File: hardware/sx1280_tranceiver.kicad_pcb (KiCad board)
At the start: 2 copper layers, 22 parts, among them J1 U.FL-R-SMT-1(80), J2 Conn_02x06_Odd_Even, U1 sx1280, U2 2450FM07D0034, Y1 ECS-520-12-37B-CTN-TR

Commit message: finalized layout
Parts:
- moved C9 2.80 mm to (84.7, 67.9)
- moved J1 2.80 mm to (86.1, 70.5)
- moved L1 2.80 mm to (86.1, 67.4)
- moved R2 2.80 mm to (86.1, 65.5)
- moved R3 2.80 mm to (86.6, 65.0)
- moved U2 2.80 mm to (84.5, 65.0)
- moved C10 2.56 mm to (89.3, 66.4)
- moved L2 2.56 mm to (88.8, 65.0)
- moved C5 2.38 mm to (80.8, 69.6)
- moved C3 2.35 mm to (79.8, 69.6)
- moved C1 2.32 mm to (78.9, 69.6)
- moved L3 2.20 mm to (76.5, 69.3)
- moved C7 2.20 mm to (79.1, 60.4)
- moved C8 2.20 mm to (75.5, 60.4)
- moved Y1 2.20 mm to (77.3, 60.4)
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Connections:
- J2 pad 12: ANT_SW -> unconnected-(J2-Pin_12-Pad12)
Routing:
- net SX_NSS: track 4.19 -> 35.5 mm
- net SX_SCK: track 3.72 -> 26.3 mm
- net SX_MOSI: track 3.84 -> 21.9 mm
- net SX_MISO: track 3.82 -> 18.2 mm
- net VBAT: track 29.2 -> 26.0 mm, vias 2 -> 1
- net Net-(AE1-FEED): track 2.49 -> 3.50 mm
- net VBAT_IO: track 4.85 -> 4.07 mm
- net Net-(U1-RFIO): track 2.72 -> 2.05 mm
- net GND: track 16.9 -> 16.7 mm, vias 11 -> 475
- added copper zone on In1.Cu, net GND
- added copper zone on In2.Cu, net GND
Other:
- board outline added: 30.5 x 16 mm
- copper layers 2 -> 4
- board text added: "sx1280_tranceiver by ihysol"

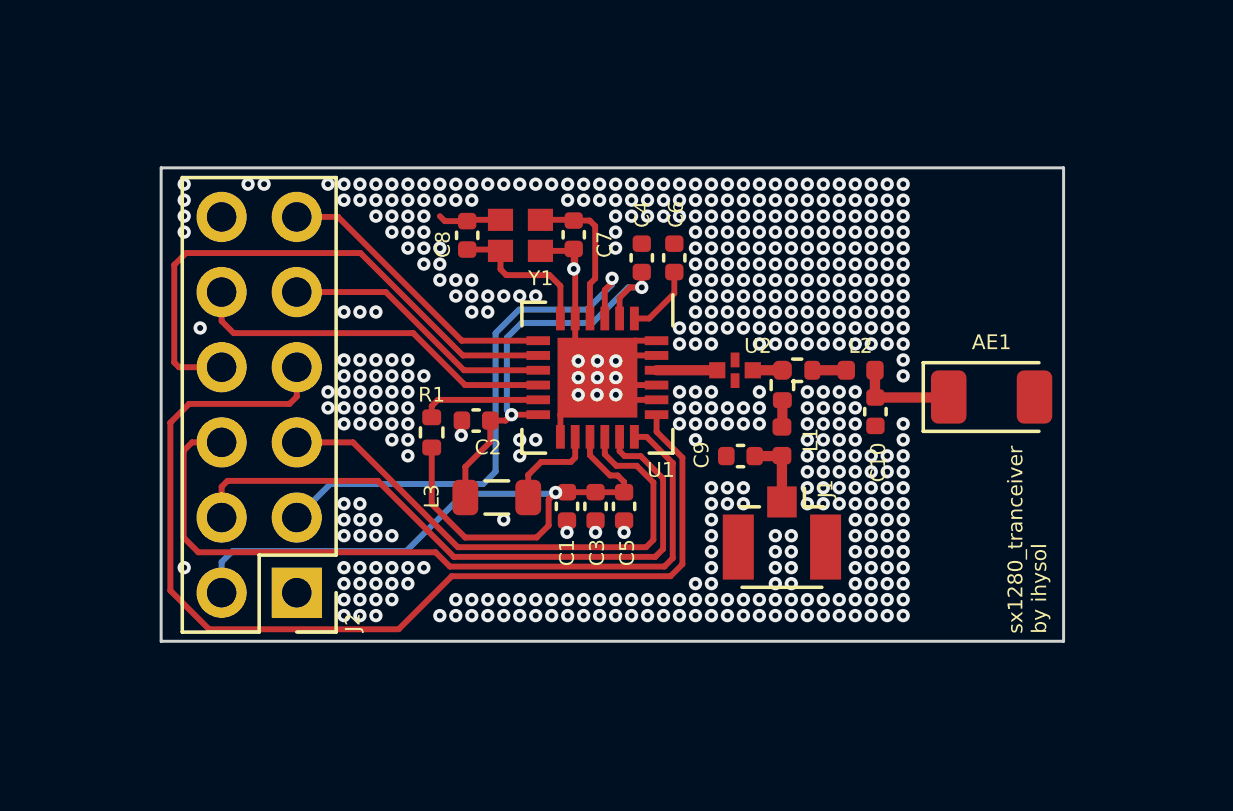
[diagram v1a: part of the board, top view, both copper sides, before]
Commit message: finalized layout, added part numbers
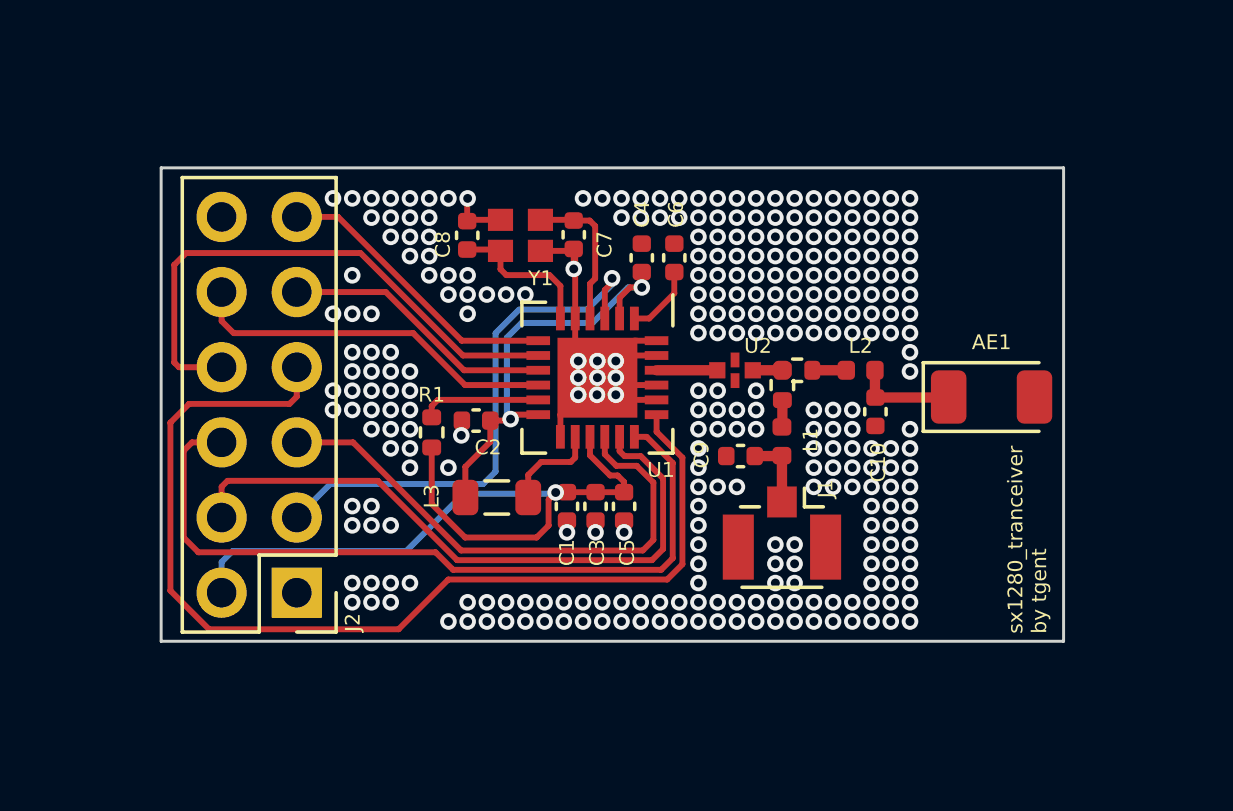
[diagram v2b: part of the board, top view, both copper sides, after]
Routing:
- net GND: track 16.7 -> 16.5 mm, vias 475 -> 304
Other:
- board text added: "sx1280_tranceiver by tgent"
- board text removed: "sx1280_tranceiver by ihysol"
